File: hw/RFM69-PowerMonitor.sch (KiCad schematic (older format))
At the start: 1 part

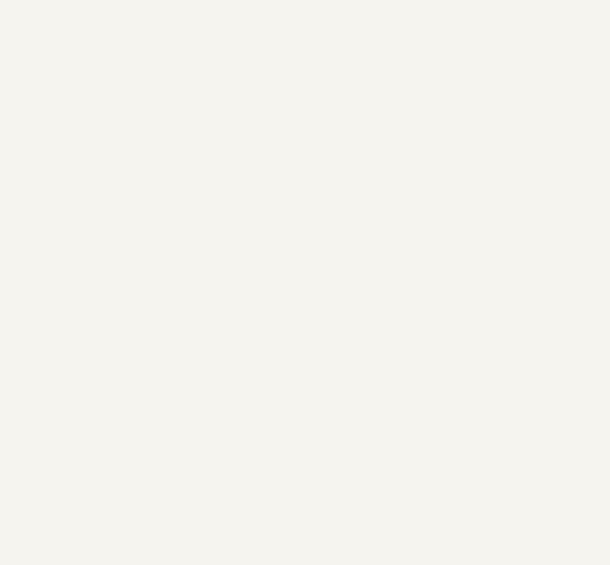
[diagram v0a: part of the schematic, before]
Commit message: Added component+footprint for the arduino mini pro.
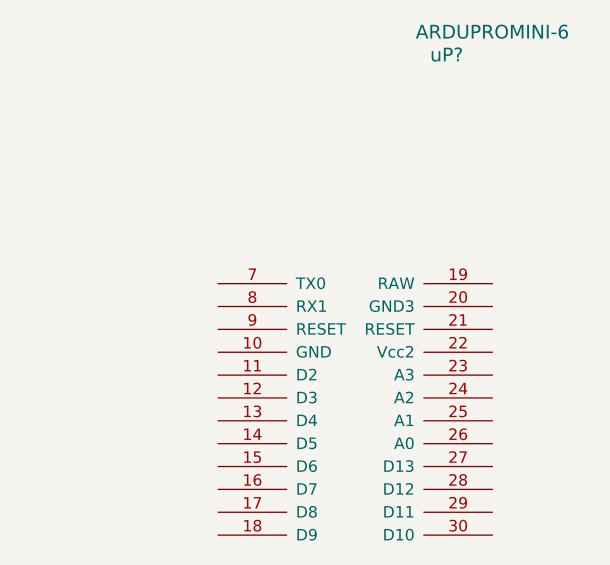
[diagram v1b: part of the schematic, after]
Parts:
- added uP?: ARDUPROMINI-6, symbol ARDUPROMINI-6
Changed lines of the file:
@@
 LIBS:valves
 LIBS:RFM69HW
+LIBS:ArduProMiniTKB
+LIBS:RFM69-PowerMonitor-cache
 EELAYER 25 0
 EELAYER END
@@
 	1    0    0    -1
 $EndComp
+$Comp
+L ARDUPROMINI-6 uP?
+U 1 1 575F2622
+P 8800 2450
+F 0 "uP?" H 8600 2350 60  0000 C CNN
+F 1 "ARDUPROMINI-6" H 8800 2450 60  0000 C CNN
+F 2 "" H 8800 2450 60  0000 C CNN
+F 3 "" H 8800 2450 60  0000 C CNN
+	1    8800 2450
+	1    0    0    -1
+$EndComp

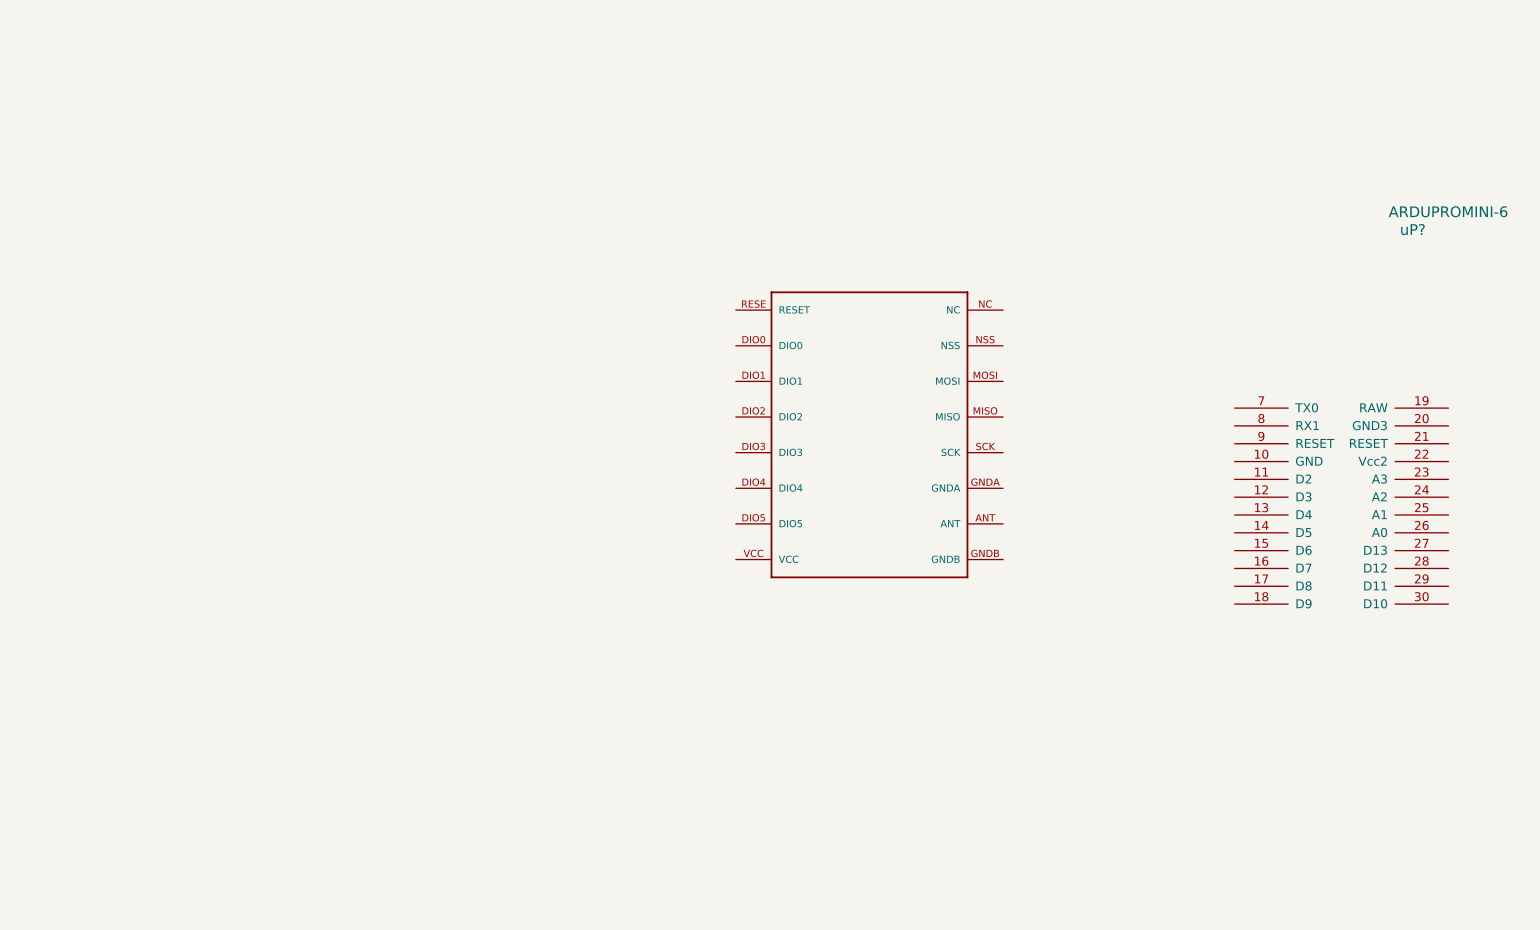
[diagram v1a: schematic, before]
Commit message: Generated netlist, assigned footprints.
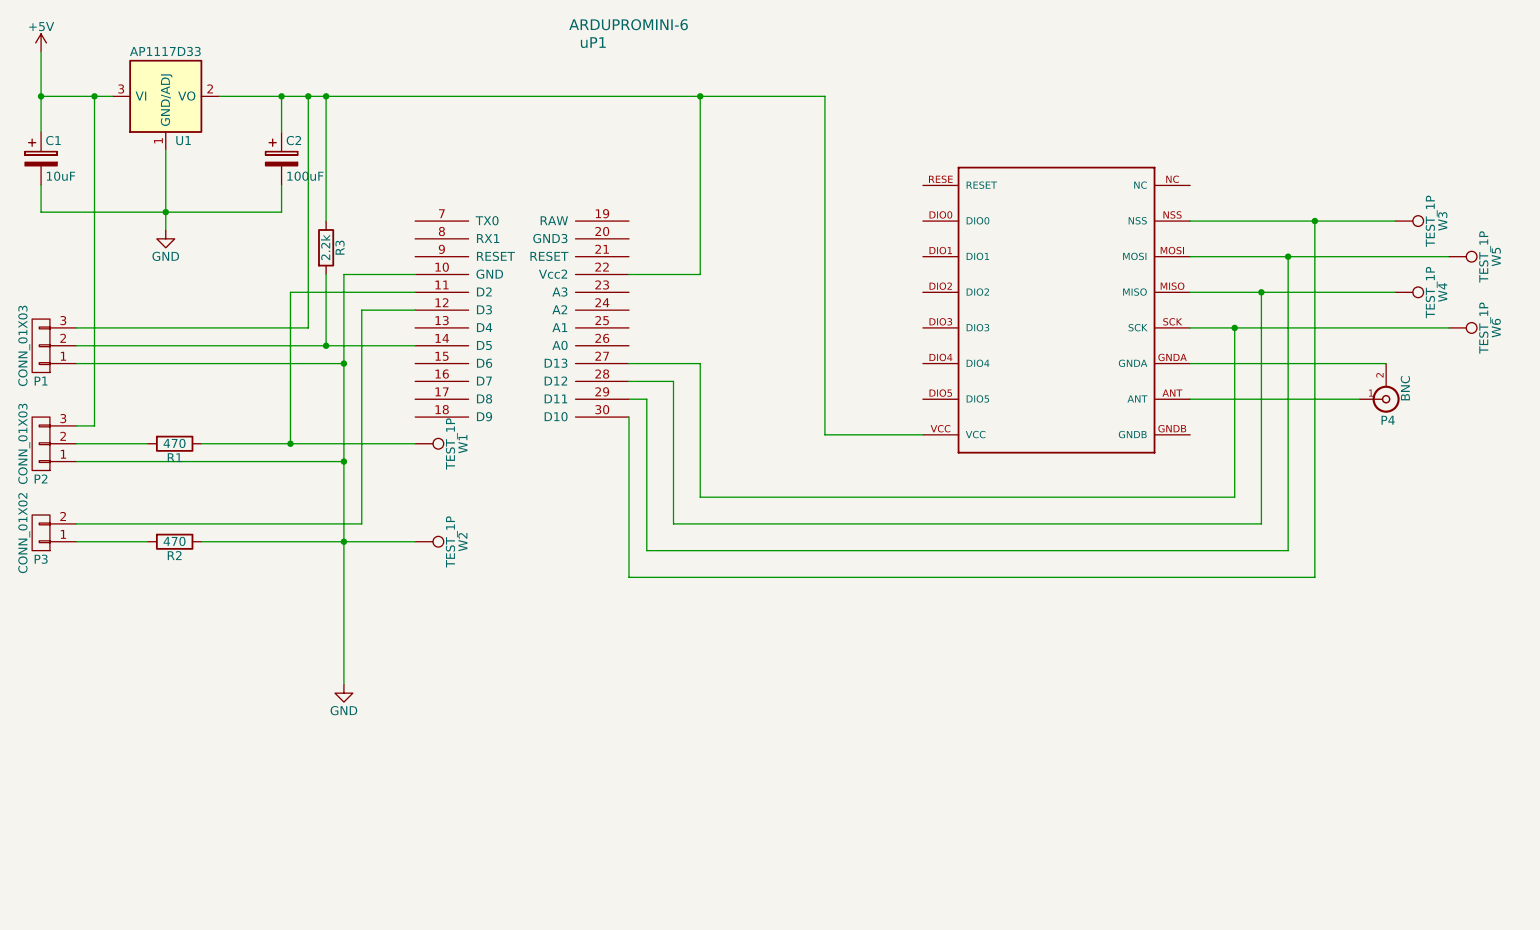
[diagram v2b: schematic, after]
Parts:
- added C1: 10uF, Capacitors_ThroughHole:C_Radial_D6.3_L11.2_P2.5, symbol CP
- added C2: 100uF, Capacitors_ThroughHole:C_Radial_D6.3_L11.2_P2.5, symbol CP
- added P1, P2: CONN_01X03, Pin_Headers:Pin_Header_Straight_1x03, symbol CONN_01X03
- added P3: CONN_01X02, Pin_Headers:Pin_Header_Straight_1x02, symbol CONN_01X02
- added P4: BNC, Connect:GS2, symbol BNC
- added R1, R2: 470, Resistors_ThroughHole:Resistor_Horizontal_RM10mm, symbol R
- added R3: 2.2k, Resistors_ThroughHole:Resistor_Horizontal_RM10mm, symbol R
- added U1: AP1117D33, TO_SOT_Packages_SMD:SOT-223, symbol AP1117D33
- added W1, W2, W3, W4, W5, W6: TEST_1P, Measurement_Points:Measurement_Point_Round-SMD-Pad_Big, symbol TEST_1P
- U2: renamed from U?; footprint RFM -> RFM69HW:RFM
- uP1: renamed from uP?; footprint (none) -> ArduProMiniTKB:ArduProMini-6
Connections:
- net at U2.ANT: now also P4.1 (In)
- net at U2.GNDA: now also P4.2 (Ext)
- net at U2.MISO: now also uP1.28 (D12), W4.1
- net at U2.MOSI: now also uP1.29 (D11), W5.1
- net at U2.NSS: now also uP1.30 (D10), W3.1
- net at U2.SCK: now also uP1.27 (D13), W6.1
- net at U2.VCC: now also uP1.22 (Vcc2), C2.1, P1.3 (P3), R3.1, U1.2 (VO)
- net GND: now reaches uP1.10 (GND)
- net GND: now also C1.2, C2.2, P1.1 (P1), P2.1 (P1), R2.1, U1.1 (GND/ADJ), W2.1
- net at uP1.11 (D2): now also R1.1, W1.1
- net at uP1.12 (D3): now also P3.2 (P2)
- net at uP1.14 (D5): now also P1.2 (P2), R3.2
- new net: P3.1 (P1), R2.2
- new net: P2.2 (P2), R1.2
- new net +5V: C1.1, P2.3 (P3), U1.3 (VI)
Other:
- moved on the sheet: uP1

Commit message: PCB done.
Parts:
- added P5: CONN_PWR, Pin_Headers:Pin_Header_Straight_1x02, symbol CONN_01X02
- P1: value CONN_01X03 -> CONN_1WIRE
- P2: value CONN_01X03 -> CONN_PIR
- P3: value CONN_01X02 -> CONN_METER
- W1: value TEST_1P -> TEST_PIR; footprint Measurement_Points:Measurement_Point_Round-SMD-Pad_Big -> Measurement_Points:Measurement_Point_Round-SMD-Pad_Small
- W2: value TEST_1P -> TEST_METER; footprint Measurement_Points:Measurement_Point_Round-SMD-Pad_Big -> Measurement_Points:Measurement_Point_Round-SMD-Pad_Small
- W3: value TEST_1P -> TEST_NSS; footprint Measurement_Points:Measurement_Point_Round-SMD-Pad_Big -> Measurement_Points:Measurement_Point_Round-SMD-Pad_Small
- W4: value TEST_1P -> TEST_MISO; footprint Measurement_Points:Measurement_Point_Round-SMD-Pad_Big -> Measurement_Points:Measurement_Point_Round-SMD-Pad_Small
- W5: value TEST_1P -> TEST_MOSI; footprint Measurement_Points:Measurement_Point_Round-SMD-Pad_Big -> Measurement_Points:Measurement_Point_Round-SMD-Pad_Small
- W6: value TEST_1P -> TEST_SCK; footprint Measurement_Points:Measurement_Point_Round-SMD-Pad_Big -> Measurement_Points:Measurement_Point_Round-SMD-Pad_Small
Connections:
- net +5V: now also P5.2 (P2)
- net GND: now also P5.1 (P1)
- net at U2.RESE (RESET): now also uP1.21 (RESET)
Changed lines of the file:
@@
 P 900 3200
 F 0 "P1" H 900 3400 50  0000 C CNN
-F 1 "CONN_01X03" V 1000 3200 50  0000 C CNN
+F 1 "CONN_1WIRE" V 1000 3200 50  0000 C CNN
 F 2 "Pin_Headers:Pin_Header_Straight_1x03" H 900 3200 50  0001 C CNN
 F 3 "" H 900 3200 50  0000 C CNN
@@
 P 900 4250
 F 0 "P3" H 900 4400 50  0000 C CNN
-F 1 "CONN_01X02" V 1000 4250 50  0000 C CNN
+F 1 "CONN_METER" V 1000 4250 50  0000 C CNN
 F 2 "Pin_Headers:Pin_Header_Straight_1x02" H 900 4250 50  0001 C CNN
 F 3 "" H 900 4250 50  0000 C CNN
@@
 P 900 3750
 F 0 "P2" H 900 3950 50  0000 C CNN
-F 1 "CONN_01X03" V 1000 3750 50  0000 C CNN
+F 1 "CONN_PIR" V 1000 3750 50  0000 C CNN
 F 2 "Pin_Headers:Pin_Header_Straight_1x03" H 900 3750 50  0001 C CNN
 F 3 "" H 900 3750 50  0000 C CNN
@@
 P 8500 2500
 F 0 "W3" H 8500 2770 50  0000 C CNN
-F 1 "TEST_1P" H 8500 2700 50  0000 C CNN
-F 2 "Measurement_Points:Measurement_Point_Round-SMD-Pad_Big" H 8700 2500 50  0001 C CNN
+F 1 "TEST_NSS" H 8500 2700 50  0000 C CNN
+F 2 "Measurement_Points:Measurement_Point_Round-SMD-Pad_Small" H 8700 2500 50  0001 C CNN
 F 3 "" H 8700 2500 50  0000 C CNN
 	1    8500 2500
@@
 P 8800 2700
 F 0 "W5" H 8800 2970 50  0000 C CNN
-F 1 "TEST_1P" H 8800 2900 50  0000 C CNN
-F 2 "Measurement_Points:Measurement_Point_Round-SMD-Pad_Big" H 9000 2700 50  0001 C CNN
+F 1 "TEST_MOSI" H 8800 2900 50  0000 C CNN
+F 2 "Measurement_Points:Measurement_Point_Round-SMD-Pad_Small" H 9000 2700 50  0001 C CNN
 F 3 "" H 9000 2700 50  0000 C CNN
 	1    8800 2700
@@
 P 8500 2900
 F 0 "W4" H 8500 3170 50  0000 C CNN
-F 1 "TEST_1P" H 8500 3100 50  0000 C CNN
-F 2 "Measurement_Points:Measurement_Point_Round-SMD-Pad_Big" H 8700 2900 50  0001 C CNN
+F 1 "TEST_MISO" H 8500 3100 50  0000 C CNN
+F 2 "Measurement_Points:Measurement_Point_Round-SMD-Pad_Small" H 8700 2900 50  0001 C CNN
 F 3 "" H 8700 2900 50  0000 C CNN
 	1    8500 2900
@@
 P 8800 3100
 F 0 "W6" H 8800 3370 50  0000 C CNN
-F 1 "TEST_1P" H 8800 3300 50  0000 C CNN
-F 2 "Measurement_Points:Measurement_Point_Round-SMD-Pad_Big" H 9000 3100 50  0001 C CNN
+F 1 "TEST_SCK" H 8800 3300 50  0000 C CNN
+F 2 "Measurement_Points:Measurement_Point_Round-SMD-Pad_Small" H 9000 3100 50  0001 C CNN
 F 3 "" H 9000 3100 50  0000 C CNN
 	1    8800 3100
@@
 P 3000 4300
 F 0 "W2" H 3000 4570 50  0000 C CNN
-F 1 "TEST_1P" H 3000 4500 50  0000 C CNN
-F 2 "Measurement_Points:Measurement_Point_Round-SMD-Pad_Big" H 3200 4300 50  0001 C CNN
+F 1 "TEST_METER" H 3000 4500 50  0000 C CNN
+F 2 "Measurement_Points:Measurement_Point_Round-SMD-Pad_Small" H 3200 4300 50  0001 C CNN
 F 3 "" H 3200 4300 50  0000 C CNN
 	1    3000 4300
@@
 P 3000 3750
 F 0 "W1" H 3000 4020 50  0000 C CNN
-F 1 "TEST_1P" H 3000 3950 50  0000 C CNN
-F 2 "Measurement_Points:Measurement_Point_Round-SMD-Pad_Big" H 3200 3750 50  0001 C CNN
+F 1 "TEST_PIR" H 3000 3950 50  0000 C CNN
+F 2 "Measurement_Points:Measurement_Point_Round-SMD-Pad_Small" H 3200 3750 50  0001 C CNN
 F 3 "" H 3200 3750 50  0000 C CNN
 	1    3000 3750
@@
 $EndComp
 Connection ~ 2300 3750
+$Comp
+L CONN_01X02 P5
+U 1 1 575FD2E0
+P 950 6050
+F 0 "P5" H 950 6200 50  0000 C CNN
+F 1 "CONN_PWR" V 1050 6050 50  0000 C CNN
+F 2 "Pin_Headers:Pin_Header_Straight_1x02" H 950 6050 50  0001 C CNN
+F 3 "" H 950 6050 50  0000 C CNN
+	1    950  6050
+	-1   0    0    1
+$EndComp
+$Comp
+L +5V #PWR04
+U 1 1 575FD338
+P 1400 5900
+F 0 "#PWR04" H 1400 5750 50  0001 C CNN
+F 1 "+5V" H 1400 6040 50  0000 C CNN
+F 2 "" H 1400 5900 50  0000 C CNN
+F 3 "" H 1400 5900 50  0000 C CNN
+	1    1400 5900
+	1    0    0    -1
+$EndComp
+$Comp
+L GND #PWR05
+U 1 1 575FD370
+P 1400 6200
+F 0 "#PWR05" H 1400 5950 50  0001 C CNN
+F 1 "GND" H 1400 6050 50  0000 C CNN
+F 2 "" H 1400 6200 50  0000 C CNN
+F 3 "" H 1400 6200 50  0000 C CNN
+	1    1400 6200
+	1    0    0    -1
+$EndComp
+Wire Wire Line
+	1150 6000 1400 6000
+Wire Wire Line
+	1400 6000 1400 5900
+Wire Wire Line
+	1150 6100 1400 6100
+Wire Wire Line
+	1400 6100 1400 6200
+Wire Wire Line
+	5850 2300 4700 2300
+Wire Wire Line
+	4700 2300 4700 2700
+Wire Wire Line
+	4700 2700 4200 2700
 $EndSCHEMATC

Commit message: Final PCB design.
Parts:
- removed P4: BNC, Connect:GS2, symbol BNC
- added P4: CONN_ANT, Connect:GS3, symbol CONN_01X03
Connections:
- net GND: now also U2.GNDA, U2.GNDB, P4.1 (P1), P4.3 (P3)
- net at U2.ANT: now also P4.2 (P2)
- net at U2.RESE (RESET): now also uP1.18 (D9); no longer uP1.21 (RESET)
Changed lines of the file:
@@
 	7350 2500 8500 2500
-$Comp
-L BNC P4
-U 1 1 575FB8E4
-P 8450 3500
-F 0 "P4" H 8460 3620 50  0000 C CNN
-F 1 "BNC" V 8560 3440 50  0000 C CNN
-F 2 "Connect:GS2" H 8450 3500 50  0001 C CNN
-F 3 "" H 8450 3500 50  0000 C CNN
-	1    8450 3500
-	1    0    0    1
-$EndComp
-Wire Wire Line
-	7350 3500 8300 3500
-Wire Wire Line
-	8450 3300 7350 3300
 $Comp
 L AP1117D33 U1
@@
 Wire Wire Line
 	1400 6100 1400 6200
-Wire Wire Line
-	5850 2300 4700 2300
-Wire Wire Line
-	4700 2300 4700 2700
-Wire Wire Line
-	4700 2700 4200 2700
+$Comp
+L CONN_01X03 P4
+U 1 1 575FF022
+P 8650 3500
+F 0 "P4" H 8650 3700 50  0000 C CNN
+F 1 "CONN_ANT" V 8750 3500 50  0000 C CNN
+F 2 "Connect:GS3" H 8650 3500 50  0001 C CNN
+F 3 "" H 8650 3500 50  0000 C CNN
+	1    8650 3500
+	1    0    0    -1
+$EndComp
+Wire Wire Line
+	7350 3500 8450 3500
+Wire Wire Line
+	8450 3400 7350 3400
+Wire Wire Line
+	7350 3400 7350 3300
+Wire Wire Line
+	8450 3600 7350 3600
+Wire Wire Line
+	7350 3600 7350 3700
+$Comp
+L GND #PWR06
+U 1 1 575FF565
+P 8300 3800
+F 0 "#PWR06" H 8300 3550 50  0001 C CNN
+F 1 "GND" H 8300 3650 50  0000 C CNN
+F 2 "" H 8300 3800 50  0000 C CNN
+F 3 "" H 8300 3800 50  0000 C CNN
+	1    8300 3800
+	1    0    0    -1
+$EndComp
+$Comp
+L GND #PWR07
+U 1 1 575FF59D
+P 8300 3200
+F 0 "#PWR07" H 8300 2950 50  0001 C CNN
+F 1 "GND" H 8300 3050 50  0000 C CNN
+F 2 "" H 8300 3200 50  0000 C CNN
+F 3 "" H 8300 3200 50  0000 C CNN
+	1    8300 3200
+	1    0    0    -1
+$EndComp
+Wire Wire Line
+	8300 3200 8300 3150
+Wire Wire Line
+	8300 3150 8200 3150
+Wire Wire Line
+	8200 3150 8200 3400
+Connection ~ 8200 3400
+Wire Wire Line
+	8300 3800 8300 3600
+Connection ~ 8300 3600
+Wire Wire Line
+	5850 2300 2800 2300
+Wire Wire Line
+	2800 2300 2800 3600
+Wire Wire Line
+	2800 3600 3000 3600
 $EndSCHEMATC
